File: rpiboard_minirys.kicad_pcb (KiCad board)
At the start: 4 copper layers, 65 x 56.5 mm, 78 parts, among them IC1 LM51231QRGRRQ1, IC2 TPS564242DRLR, J1 Conn_01x01_Pin, J2 Conn_01x01_Pin, J3 Conn_01x01_Pin, J4 Conn_01x01_Pin, J6 MCU_Connector, J7 RPi_GPIO, Q1 ISK057N04LM6ATLA1, Q2 ISK057N04LM6ATLA1

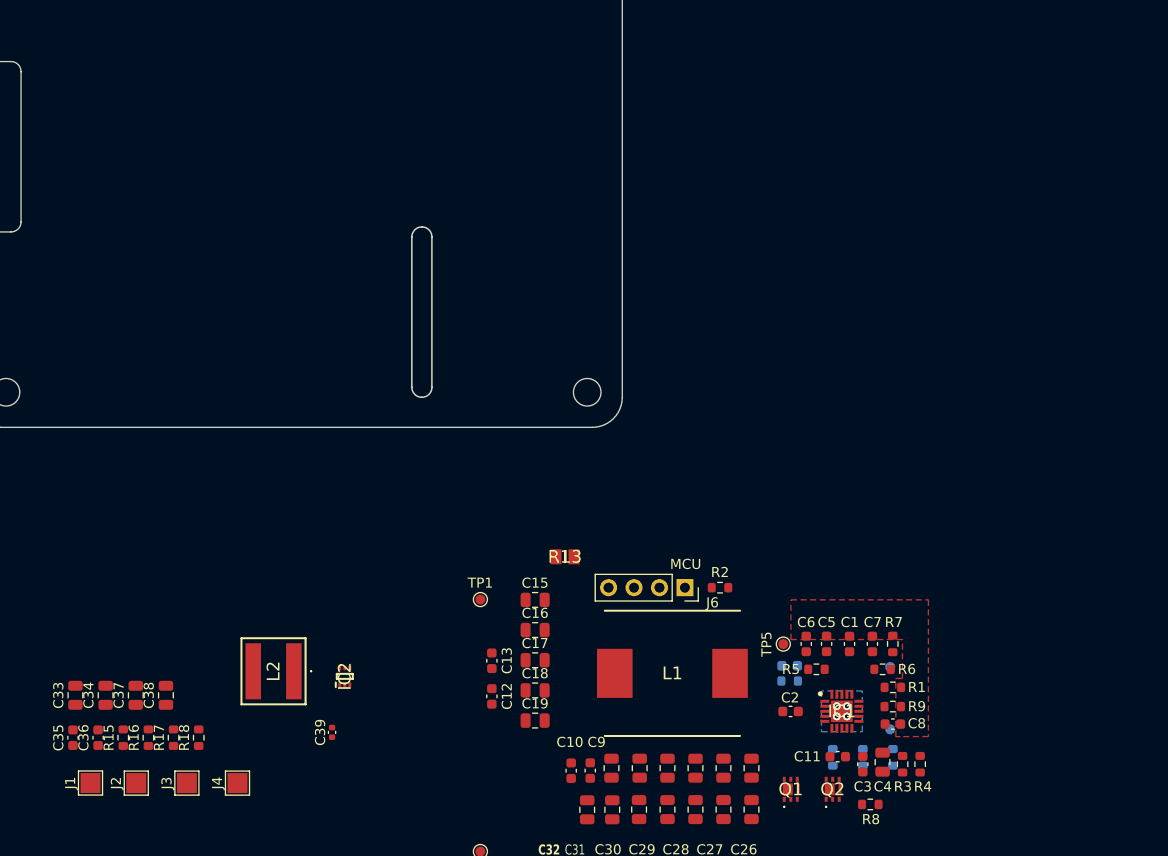
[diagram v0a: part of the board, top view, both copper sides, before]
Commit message: Added required connectors for this version
Also did some file name changes
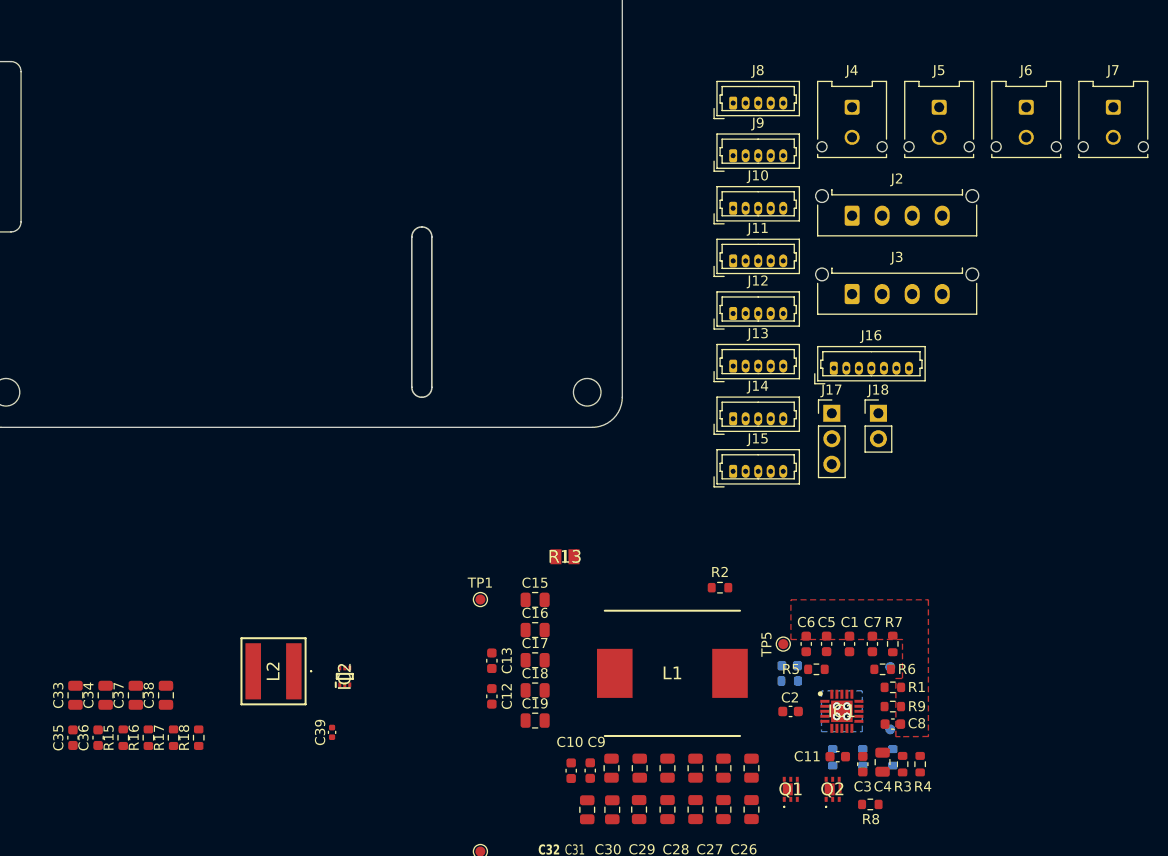
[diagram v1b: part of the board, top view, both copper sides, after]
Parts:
- removed the J1 at (117.4, 146.2)
- added J10: ToF1_Sensor, Connector_Molex:Molex_PicoBlade_53047-0510_1x05_P1.25mm_Vertical, F.Cu at (181.6, 88.9)
- added J11: ToF2_Sensor, Connector_Molex:Molex_PicoBlade_53047-0510_1x05_P1.25mm_Vertical, F.Cu at (181.6, 94.1)
- added J12: ToF3_Sensor, Connector_Molex:Molex_PicoBlade_53047-0510_1x05_P1.25mm_Vertical, F.Cu at (181.6, 99.4)
- added J13: ToF4_Sensor, Connector_Molex:Molex_PicoBlade_53047-0510_1x05_P1.25mm_Vertical, F.Cu at (181.6, 104.6)
- added J14: ToF5_Sensor, Connector_Molex:Molex_PicoBlade_53047-0510_1x05_P1.25mm_Vertical, F.Cu at (181.6, 109.9)
- added J15: ToF6_Sensor, Connector_Molex:Molex_PicoBlade_53047-0510_1x05_P1.25mm_Vertical, F.Cu at (181.6, 115.1)
- added J16: SPI_Interface, Connector_Molex:Molex_PicoBlade_53047-0710_1x07_P1.25mm_Vertical, F.Cu at (191.6, 104.8)
- added J17: UART_Interface, Connector_PinHeader_2.54mm:PinHeader_1x03_P2.54mm_Vertical, F.Cu at (191.4, 109.3)
- added J18: Fan_Interface, Connector_PinHeader_2.54mm:PinHeader_1x02_P2.54mm_Vertical, F.Cu at (196.1, 109.3)
- added J5: B_Cell_2, Connector_Molex:Molex_Micro-Fit_3.0_43045-0212_2x01_P3.00mm_Vertical, F.Cu at (202.1, 78.8)
- added J7: SW, Connector_Molex:Molex_Micro-Fit_3.0_43045-0212_2x01_P3.00mm_Vertical, F.Cu at (219.5, 78.8)
- added J8: Temp_Sensor, Connector_Molex:Molex_PicoBlade_53047-0510_1x05_P1.25mm_Vertical, F.Cu at (181.6, 78.4)
- added J9: IMU_Sensor, Connector_Molex:Molex_PicoBlade_53047-0510_1x05_P1.25mm_Vertical, F.Cu at (181.6, 83.6)
- J2: value Conn_01x01_Pin -> Motor_L; footprint TestPoint:TestPoint_Pad_2.0x2.0mm -> Connector_Molex:Molex_Micro-Fit_3.0_43650-0415_1x04_P3.00mm_Vertical
- J3: value Conn_01x01_Pin -> Motor_R; footprint TestPoint:TestPoint_Pad_2.0x2.0mm -> Connector_Molex:Molex_Micro-Fit_3.0_43650-0415_1x04_P3.00mm_Vertical
- J4: value Conn_01x01_Pin -> B_Cell_3; footprint TestPoint:TestPoint_Pad_2.0x2.0mm -> Connector_Molex:Molex_Micro-Fit_3.0_43045-0212_2x01_P3.00mm_Vertical
- J6: value MCU_Connector -> B_Cell_1; footprint Connector_PinSocket_2.54mm:PinSocket_1x04_P2.54mm_Vertical -> Connector_Molex:Molex_Micro-Fit_3.0_43045-0212_2x01_P3.00mm_Vertical
- moved J4 91.2 mm to (193.4, 78.8), turned to 0 degrees
- moved J2 91.1 mm to (193.4, 89.6), turned to 0 degrees
- moved J3 82.4 mm to (193.4, 97.5), turned to 0 degrees
- moved J6 58.8 mm to (210.8, 78.8), turned to 0 degrees
- renumbered J7 to J1
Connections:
- net /5V_Logic_Power/5V renamed /Connectors/+5V
- J2 pad 1: /5V -> unconnected-(J2-Pin_1-Pad1)
- J3 pad 1: GND -> unconnected-(J3-Pin_1-Pad1)
- J4 pad 1: VCC -> unconnected-(J4-Pin_1-Pad1)
- J6 pad 1: /PGOOD -> unconnected-(J6-Pin_1-Pad1)
- J6 pad 2: /VCC_MCU -> unconnected-(J6-Pin_2-Pad2)
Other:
- board text removed: "MCU"

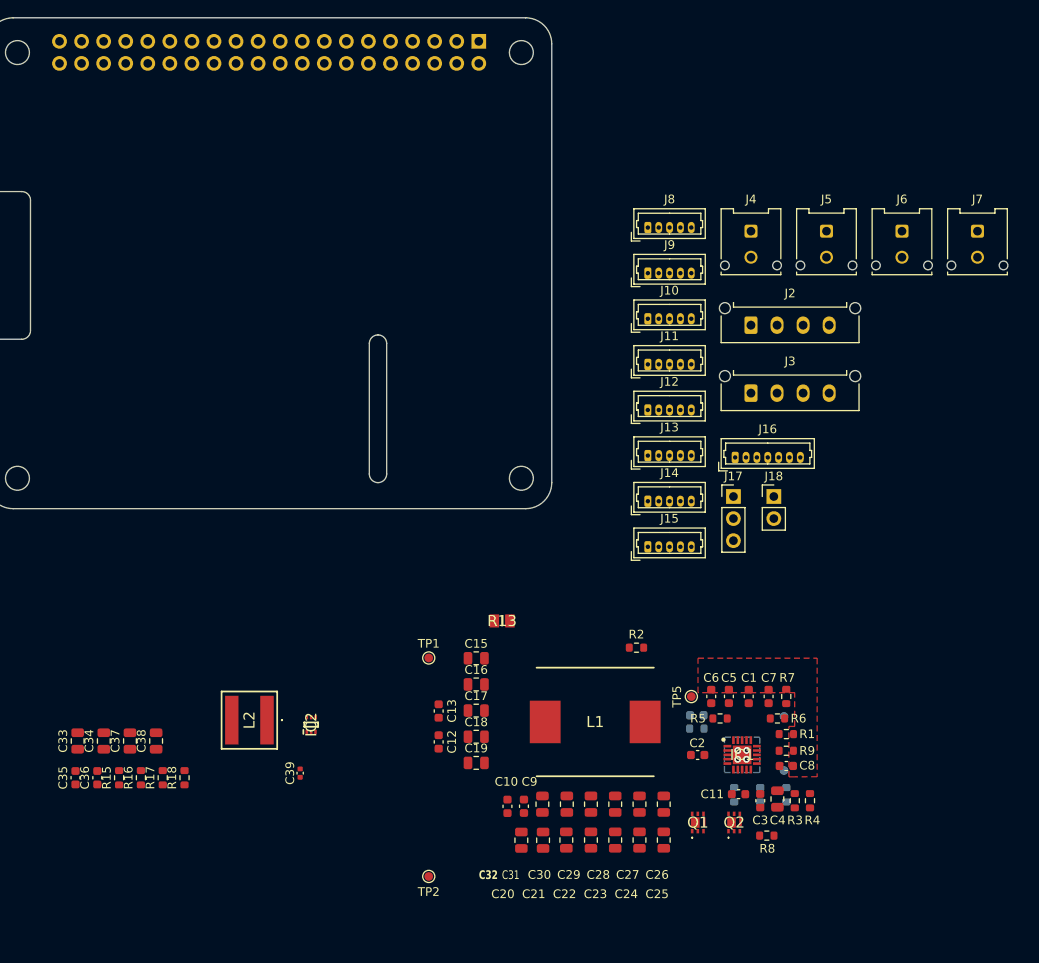
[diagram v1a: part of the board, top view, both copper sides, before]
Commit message: Finished motor drivers schematic
Still need to connect all the connectors and sort out old unused connections
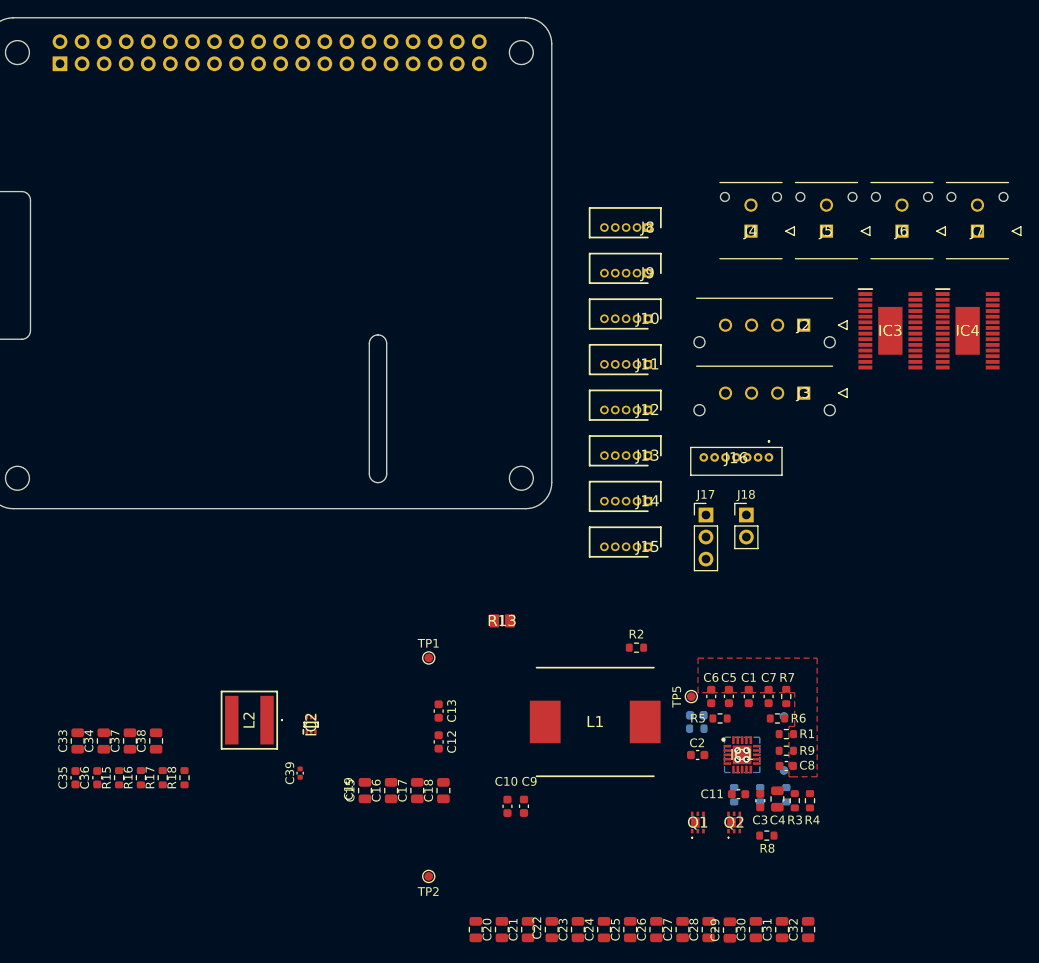
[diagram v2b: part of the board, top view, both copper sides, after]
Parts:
- added IC3: L6470HTR, parts:SOP65P640X120-29N, F.Cu at (209.5, 90.3)
- added IC4: L6470HTR, parts:SOP65P640X120-29N, F.Cu at (218.4, 90.3)
- J10, J11, J12, J13, J14, J15, J8, J9: footprint Connector_Molex:Molex_PicoBlade_53047-0510_1x05_P1.25mm_Vertical -> parts:SHDR5W27P0X125_1X5_800X320X440P
- J16: footprint Connector_Molex:Molex_PicoBlade_53047-0710_1x07_P1.25mm_Vertical -> parts:530470710
- J2, J3: footprint Connector_Molex:Molex_Micro-Fit_3.0_43650-0415_1x04_P3.00mm_Vertical -> parts:43650-04YY_151617
- J4, J5, J6, J7: footprint Connector_Molex:Molex_Micro-Fit_3.0_43045-0212_2x01_P3.00mm_Vertical -> parts:43045-02YY_121314
- moved J1 48.3 mm to (113.9, 59.5), turned to -90 degrees
- moved C32 34.6 mm to (200.0, 159.2), turned to 90 degrees
- moved C31 29.4 mm to (197.0, 159.2), turned to 90 degrees
- moved C30 24.1 mm to (194.0, 159.2), turned to 90 degrees
- moved C15 19.9 mm to (149.0, 143.2), turned to 90 degrees
- moved C19 19.2 mm to (161.8, 159.2), turned to 90 degrees
- moved C29 19.1 mm to (191.0, 159.2), turned to 90 degrees
- moved C16 15.7 mm to (152.0, 143.2), turned to 90 degrees
- moved C20 15.2 mm to (164.8, 159.2)
- moved C22 15.1 mm to (170.5, 159.2)
- moved C21 15.1 mm to (167.8, 159.2)
- moved C23 15.1 mm to (173.5, 159.2)
- moved C24 15.0 mm to (176.5, 159.2)
- moved C25 14.9 mm to (179.5, 159.2)
- moved C28 14.9 mm to (188.6, 159.2), turned to 90 degrees
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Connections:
- net /COMP renamed /Supply_24V/COMP
- net /CSN renamed /Supply_24V/CSN
- net /Connectors/+5V renamed /Supply_5V/+5V
- net /HB renamed /Supply_24V/HB
- net /HO renamed /Supply_24V/HO
- net /LO renamed /Supply_24V/LO
- net /MCU_EN renamed /Supply_24V/MCU_EN
- net /MODE renamed /Supply_24V/MODE
- net /PGOOD renamed /Supply_24V/PGOOD
- net /SW renamed /Supply_24V/SW
- net /TRK renamed /Supply_24V/TRK
- net /UVLO renamed /Supply_24V/UVLO
- net /VCC_DRIVER renamed /Supply_24V/VCC_DRIVER
- net /VCC_MCU renamed /Supply_24V/VCC_MCU
- net /VOUT renamed /Supply_24V/VOUT
- net /VREF renamed /Supply_24V/VREF
